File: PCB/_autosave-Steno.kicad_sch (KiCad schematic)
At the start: 111 parts, among them J1 USB-C USB 2.0 MC-372, Q1 AO3407, SW1 SW_Push_Dual, SW10 H, SW11 R, SW12 O, SW13 *, SW14 E, SW15 #, SW16 F, SW17 R, SW18 U, SW19 P, SW2 #, SW20 B, SW21 *, SW22 #, SW23 L, SW24 G, SW25 T, SW26 S, SW27 D, SW28 Z, SW3 S, SW4 T, SW5 K, SW6 #, SW7 P, SW8 W, SW9 A, U1 BQ27427, U2 BQ24075RGT, U3 MAX16054, U4 TPS709, U5 Conn_01x14_Socket, U6 nRF52840_aQFN73, U7 SSD1306, X1 32.768 kHz, X2 32MHZ

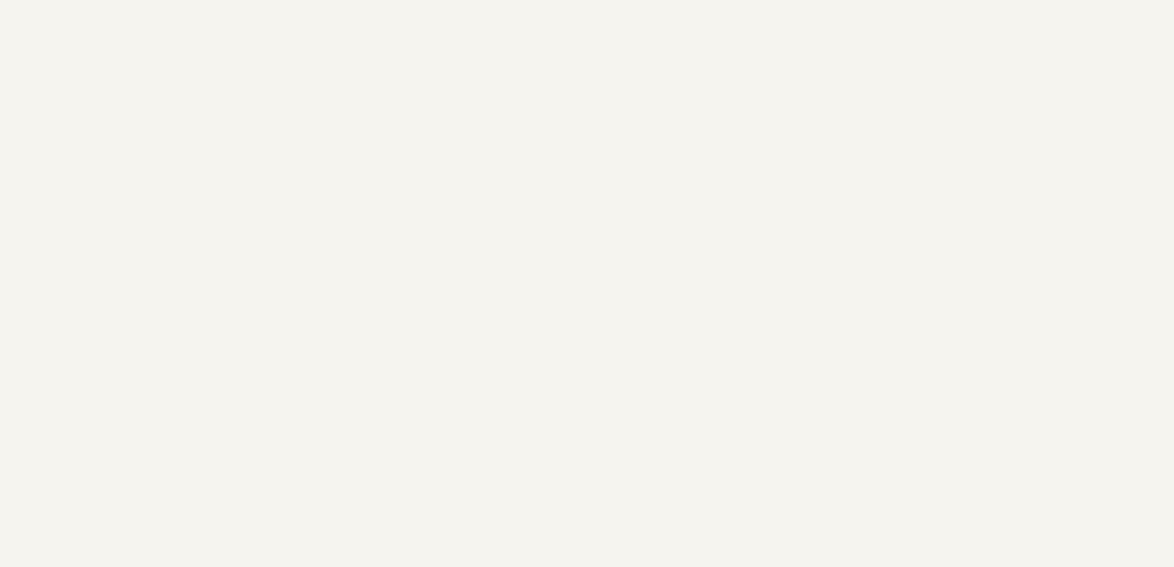
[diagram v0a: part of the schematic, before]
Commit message: show battery percentage
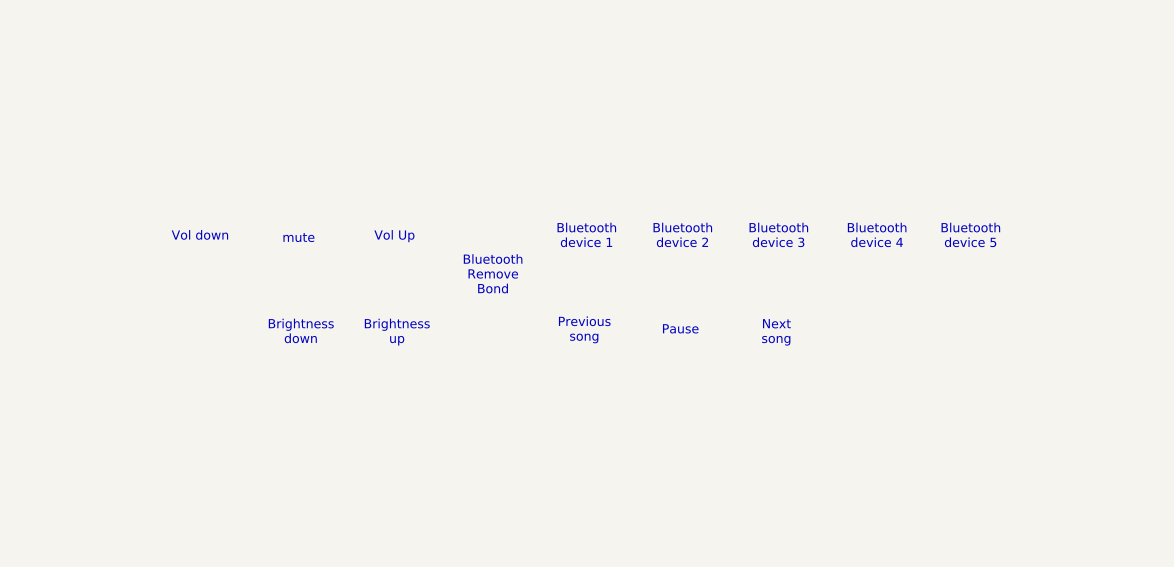
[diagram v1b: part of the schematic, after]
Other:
- note added: "Bluetooth Remove Bond"
- note added: "Bluetooth device 1"
- note added: "Bluetooth device 2"
- note added: "Bluetooth device 3"
- note added: "Bluetooth device 4"
- note added: "Bluetooth device 5"
- note added: "Brightness down"
- note added: "Brightness up"
- note added: "Next song"
- note added: "Pause"
- note added: "Previous song"
- note added: "Vol Up"
- note added: "Vol down"
- note added: "mute"
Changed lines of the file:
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@@
 	(generator_version "9.0")
 	(paper "A4")
+	(text "Previous\nsong"
+		(exclude_from_sim no)
+		(at 469.392 100.33 0)
+		(effects
+			(font
+				(size 1.016 1.016)
+				(color 0 0 0 1)
+			)
+		)
+	)
+	(text "Bluetooth \ndevice 4"
+		(exclude_from_sim no)
+		(at 501.904 89.916 0)
+		(effects
+			(font
+				(size 1.016 1.016)
+				(color 0 0 0 1)
+			)
+		)
+	)
+	(text "Bluetooth \ndevice 2"
+		(exclude_from_sim no)
+		(at 480.314 89.916 0)
+		(effects
+			(font
+				(size 1.016 1.016)
+				(color 0 0 0 1)
+			)
+		)
+	)
+	(text "Next\nsong"
+		(exclude_from_sim no)
+		(at 490.728 100.584 0)
+		(effects
+			(font
+				(size 1.016 1.016)
+				(color 0 0 0 1)
+			)
+		)
+	)
 	(text "USB charge in"
 		(exclude_from_sim no)
@@
 		)
 	)
+	(text "Pause"
+		(exclude_from_sim no)
+		(at 480.06 100.33 0)
+		(effects
+			(font
+				(size 1.016 1.016)
+				(color 0 0 0 1)
+			)
+		)
+	)
+	(text "Bluetooth \ndevice 3"
+		(exclude_from_sim no)
+		(at 490.982 89.916 0)
+		(effects
+			(font
+				(size 1.016 1.016)
+				(color 0 0 0 1)
+			)
+		)
+	)
+	(text "Brightness \ndown"
+		(exclude_from_sim no)
+		(at 437.896 100.584 0)
+		(effects
+			(font
+				(size 1.016 1.016)
+				(color 0 0 0 1)
+			)
+		)
+	)
 	(text "3V REGULATOR"
 		(exclude_from_sim no)
@@
 			(font
 				(size 1.27 1.27)
+			)
+		)
+	)
+	(text "Bluetooth \ndevice 5"
+		(exclude_from_sim no)
+		(at 512.318 89.916 0)
+		(effects
+			(font
+				(size 1.016 1.016)
+				(color 0 0 0 1)
+			)
+		)
+	)
+	(text "Brightness \nup"
+		(exclude_from_sim no)
+		(at 448.564 100.584 0)
+		(effects
+			(font
+				(size 1.016 1.016)
+				(color 0 0 0 1)
+			)
+		)
+	)
+	(text "Bluetooth \ndevice 1"
+		(exclude_from_sim no)
+		(at 469.646 89.916 0)
+		(effects
+			(font
+				(size 1.016 1.016)
+				(color 0 0 0 1)
 			)
 		)
@@
 		)
 	)
+	(text "mute"
+		(exclude_from_sim no)
+		(at 437.642 90.17 0)
+		(effects
+			(font
+				(size 1.016 1.016)
+				(color 0 0 0 1)
+			)
+		)
+	)
+	(text "Vol Up"
+		(exclude_from_sim no)
+		(at 448.31 89.916 0)
+		(effects
+			(font
+				(size 1.016 1.016)
+				(color 0 0 0 1)
+			)
+		)
+	)
+	(text "Vol down"
+		(exclude_from_sim no)
+		(at 426.72 89.916 0)
+		(effects
+			(font
+				(size 1.016 1.016)
+				(color 0 0 0 1)
+			)
+		)
+	)
+	(text "Bluetooth \nRemove \nBond"
+		(exclude_from_sim no)
+		(at 459.232 94.234 0)
+		(effects
+			(font
+				(size 1.016 1.016)
+				(color 0 0 0 1)
+			)
+		)
+	)
